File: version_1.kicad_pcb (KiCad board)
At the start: 2 copper layers, 100 x 120 mm, 101 parts, among them CN1 B6B-PH-K-S(LF)(SN), CN2 B6B-PH-K-S(LF)(SN), CN3 B6B-PH-K-S(LF)(SN), CN4 B6B-PH-K-S(LF)(SN), M5 Motor_Servo_JR, M6 Motor_Servo_JR, M7 Motor_Servo_JR, M8 Motor_Servo_JR, Q17 AO3401A, Q18 AO3401A, Q19 AO3401A, Q20 AO3401A, Q21 AO3400A, Q22 AO3400A, Q23 AO3400A, Q24 AO3400A, Q25 AO3400A, U1 Pico, U10 74HCT595D, U12 C967633, U13 DRV8870DDA, U15 DRV8870DDA, U16 DRV8870DDA, U17 DRV8870DDA, U18 SM04B-SRSS-TB_(LF)(SN), U2 SS-12D10L5, U3 L7805CD2T-TR, U4 TPS562209DDCR, U5 FXL0530-4R7-M, U6 BH-18650-B5BA016

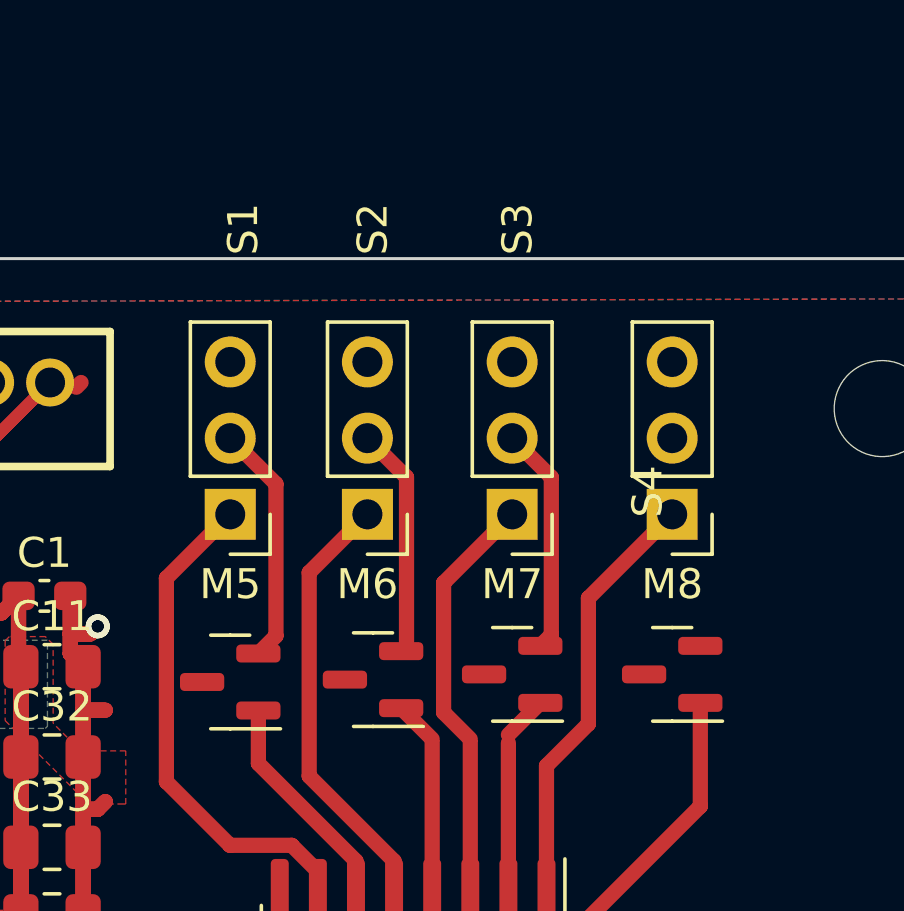
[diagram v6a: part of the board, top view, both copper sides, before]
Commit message: fliped servo mosfets
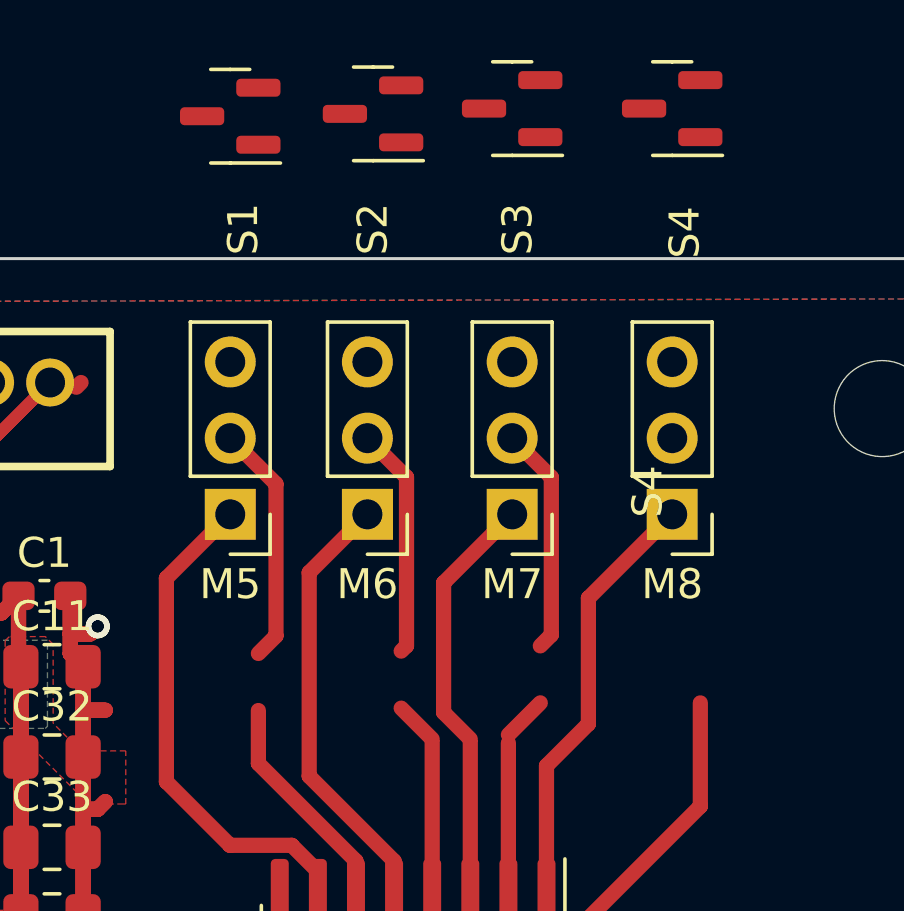
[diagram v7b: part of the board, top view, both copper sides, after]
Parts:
- moved Q17 18.9 mm to (93.3, 15.3)
- moved Q18 18.9 mm to (98.0, 15.2)
- moved Q19 18.9 mm to (102.7, 15.0)
- moved Q20 18.9 mm to (108.0, 15.0)
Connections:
- Q17 pad 2: Net-(M5-+) -> +5V
- Q17 pad 3: +5V -> Net-(M5-+)
- Q18 pad 2: Net-(M6-+) -> +5V
- Q18 pad 3: +5V -> Net-(M6-+)
- Q19 pad 2: Net-(M7-+) -> +5V
- Q19 pad 3: +5V -> Net-(M7-+)
- Q20 pad 2: Net-(M8-+) -> +5V
- Q20 pad 3: +5V -> Net-(M8-+)
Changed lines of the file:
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@@
   )
   (footprint "Package_TO_SOT_SMD:SOT-23" (layer "F.Cu")
-    (at 93.268 34.113 180)
+    (at 93.268 15.254 180)
     (descr "SOT, 3 Pin (https://www.jedec.org/system/files/docs/to-236h.pdf variant AB), generated with kicad-footprint-generator ipc_gullwing_generator.py")
     (tags "SOT TO_SOT_SMD")
@@
       (net 3 "/Untitled Sheet7/PWR") (pinfunction "G") (pintype "input"))
     (pad "2" smd roundrect (at -0.9375 0.95 180) (size 1.475 0.6) (layers "F.Cu" "F.Paste" "F.Mask") (roundrect_rratio 0.25)
-      (net 52 "Net-(M5-+)") (pinfunction "S") (pintype "passive"))
+      (net 4 "+5V") (pinfunction "S") (pintype "passive"))
     (pad "3" smd roundrect (at 0.9375 0 180) (size 1.475 0.6) (layers "F.Cu" "F.Paste" "F.Mask") (roundrect_rratio 0.25)
-      (net 4 "+5V") (pinfunction "D") (pintype "passive"))
+      (net 52 "Net-(M5-+)") (pinfunction "D") (pintype "passive"))
     (model "${KICAD6_3DMODEL_DIR}/Package_TO_SOT_SMD.3dshapes/SOT-23.wrl"
       (offset (xyz 0 0 0))
@@
   )
   (footprint "Package_TO_SOT_SMD:SOT-23" (layer "F.Cu")
-    (at 98.028 34.0345 180)
+    (at 98.028 15.1755 180)
     (descr "SOT, 3 Pin (https://www.jedec.org/system/files/docs/to-236h.pdf variant AB), generated with kicad-footprint-generator ipc_gullwing_generator.py")
     (tags "SOT TO_SOT_SMD")
@@
       (net 5 "/Untitled Sheet4/PWR") (pinfunction "G") (pintype "input"))
     (pad "2" smd roundrect (at -0.9375 0.95 180) (size 1.475 0.6) (layers "F.Cu" "F.Paste" "F.Mask") (roundrect_rratio 0.25)
-      (net 6 "Net-(M6-+)") (pinfunction "S") (pintype "passive"))
+      (net 4 "+5V") (pinfunction "S") (pintype "passive"))
     (pad "3" smd roundrect (at 0.9375 0 180) (size 1.475 0.6) (layers "F.Cu" "F.Paste" "F.Mask") (roundrect_rratio 0.25)
-      (net 4 "+5V") (pinfunction "D") (pintype "passive"))
+      (net 6 "Net-(M6-+)") (pinfunction "D") (pintype "passive"))
     (model "${KICAD6_3DMODEL_DIR}/Package_TO_SOT_SMD.3dshapes/SOT-23.wrl"
       (offset (xyz 0 0 0))
@@
   )
   (footprint "Package_TO_SOT_SMD:SOT-23" (layer "F.Cu")
-    (at 108 33.859 180)
+    (at 108 15 180)
     (descr "SOT, 3 Pin (https://www.jedec.org/system/files/docs/to-236h.pdf variant AB), generated with kicad-footprint-generator ipc_gullwing_generator.py")
     (tags "SOT TO_SOT_SMD")
@@
       (net 70 "/Servo/PWR") (pinfunction "G") (pintype "input"))
     (pad "2" smd roundrect (at -0.9375 0.95 180) (size 1.475 0.6) (layers "F.Cu" "F.Paste" "F.Mask") (roundrect_rratio 0.25)
-      (net 8 "Net-(M8-+)") (pinfunction "S") (pintype "passive"))
+      (net 4 "+5V") (pinfunction "S") (pintype "passive"))
     (pad "3" smd roundrect (at 0.9375 0 180) (size 1.475 0.6) (layers "F.Cu" "F.Paste" "F.Mask") (roundrect_rratio 0.25)
-      (net 4 "+5V") (pinfunction "D") (pintype "passive"))
+      (net 8 "Net-(M8-+)") (pinfunction "D") (pintype "passive"))
     (model "${KICAD6_3DMODEL_DIR}/Package_TO_SOT_SMD.3dshapes/SOT-23.wrl"
       (offset (xyz 0 0 0))
@@
   )
   (footprint "Package_TO_SOT_SMD:SOT-23" (layer "F.Cu")
-    (at 102.666 33.859 180)
+    (at 102.666 15 180)
     (descr "SOT, 3 Pin (https://www.jedec.org/system/files/docs/to-236h.pdf variant AB), generated with kicad-footprint-generator ipc_gullwing_generator.py")
     (tags "SOT TO_SOT_SMD")
@@
       (net 69 "/Servo2/PWR") (pinfunction "G") (pintype "input"))
     (pad "2" smd roundrect (at -0.9375 0.95 180) (size 1.475 0.6) (layers "F.Cu" "F.Paste" "F.Mask") (roundrect_rratio 0.25)
-      (net 7 "Net-(M7-+)") (pinfunction "S") (pintype "passive"))
+      (net 4 "+5V") (pinfunction "S") (pintype "passive"))
     (pad "3" smd roundrect (at 0.9375 0 180) (size 1.475 0.6) (layers "F.Cu" "F.Paste" "F.Mask") (roundrect_rratio 0.25)
-      (net 4 "+5V") (pinfunction "D") (pintype "passive"))
+      (net 7 "Net-(M7-+)") (pinfunction "D") (pintype "passive"))
     (model "${KICAD6_3DMODEL_DIR}/Package_TO_SOT_SMD.3dshapes/SOT-23.wrl"
       (offset (xyz 0 0 0))
@@
     (effects (font (size 1 1) (thickness 0.15)) (justify left bottom))
   )
+  (gr_text "S4" (at 109 20 90) (layer "F.SilkS")
+    (effects (font (size 1 1) (thickness 0.15)) (justify left bottom))
+  )

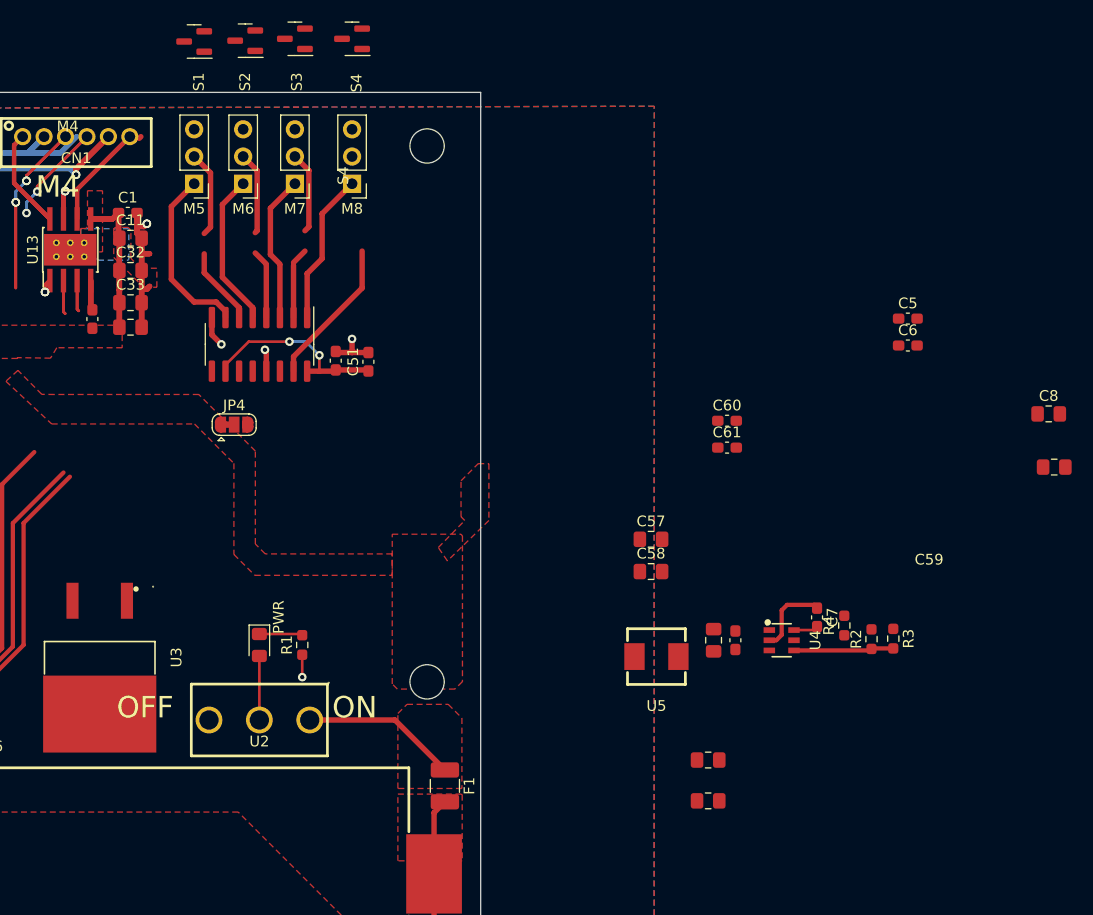
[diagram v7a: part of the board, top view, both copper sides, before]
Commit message: new servo routing
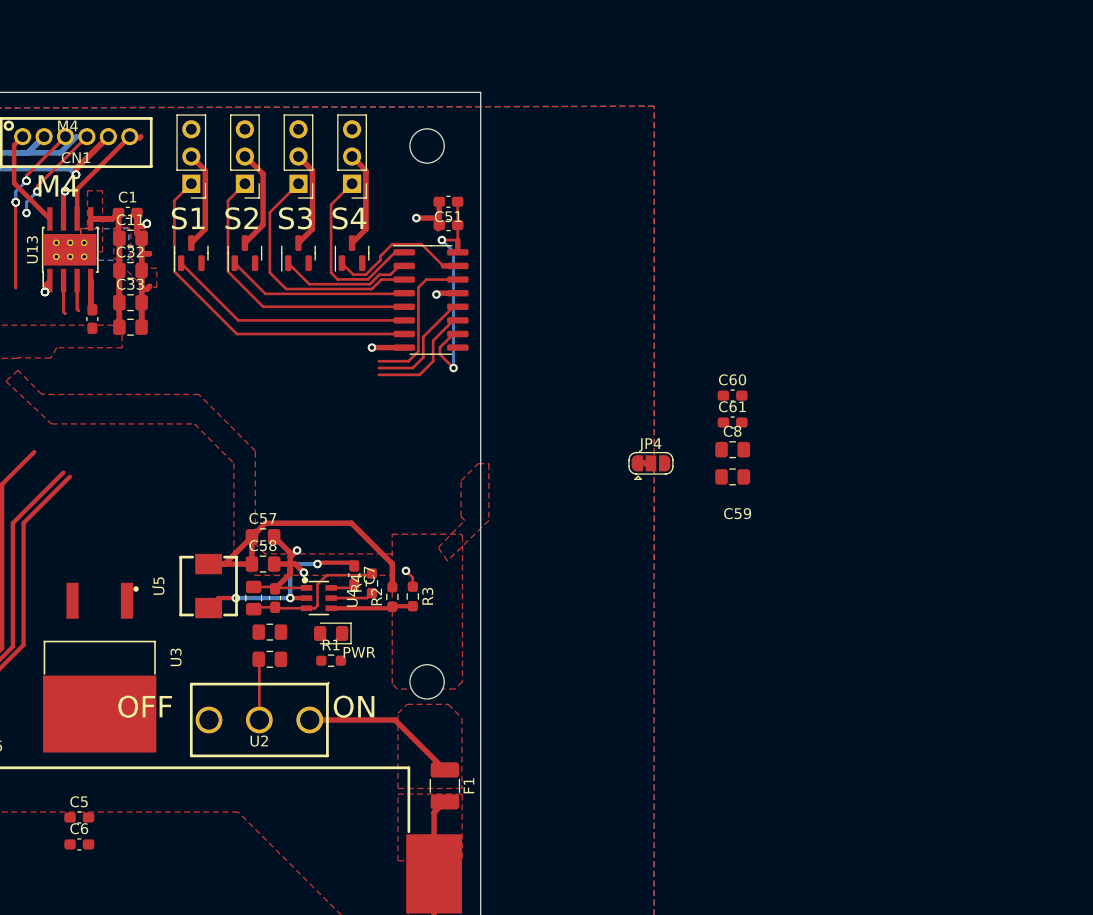
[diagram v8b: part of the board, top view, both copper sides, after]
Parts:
- moved C5 90.2 mm to (82.5, 87.7)
- moved C6 90.2 mm to (82.5, 90.2)
- moved R3 45.0 mm to (113.7, 67.0)
- moved R2 44.9 mm to (111.8, 67.1)
- moved R4 44.2 mm to (109.9, 65.8)
- moved U4 43.4 mm to (104.9, 67.2)
- moved C7 43.4 mm to (108.2, 65.1)
- moved C14 43.1 mm to (100.8, 67.2)
- moved C31 43.1 mm to (98.8, 67.2)
- moved C30 43.0 mm to (100.3, 72.9)
- moved C13 42.6 mm to (100.3, 70.4)
- moved U5 42.3 mm to (94.6, 66.1), turned to 90 degrees
- moved JP4 39.1 mm to (135.9, 54.6)
- moved C58 36.2 mm to (99.7, 64.0)
- moved C57 36.2 mm to (99.7, 61.5)
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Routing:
- net Net-(JP4-A): track 0.00 -> 29.0 mm
- net Net-(M8-+): track 0.00 -> 16.5 mm
- net /Untitled Sheet7/PWM: track 16.7 -> 32.7 mm
- net GND: track 149.2 -> 165.1 mm, vias 37 -> 39
- net /Untitled Sheet7/PWR: track 7.30 -> 23.1 mm
- net /PWM_DATA: track 58.0 -> 72.0 mm
- net VCC: track 115.3 -> 128.5 mm
- net /Untitled Sheet4/PWM: track 14.5 -> 26.6 mm
- net Net-(U4-SW): track 7.29 -> 18.9 mm, vias 0 -> 3
- net /PWM_CS: track 62.4 -> 73.2 mm
- net /Untitled Sheet4/PWR: track 6.33 -> 17.0 mm
- net /PWM_CLK: track 57.0 -> 67.6 mm
- net /Servo2/PWM: track 13.7 -> 22.9 mm
- net /Servo2/PWR: track 6.37 -> 12.3 mm
- net +5V: track 37.6 -> 42.8 mm
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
